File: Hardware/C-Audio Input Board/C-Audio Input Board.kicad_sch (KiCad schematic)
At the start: 5 parts

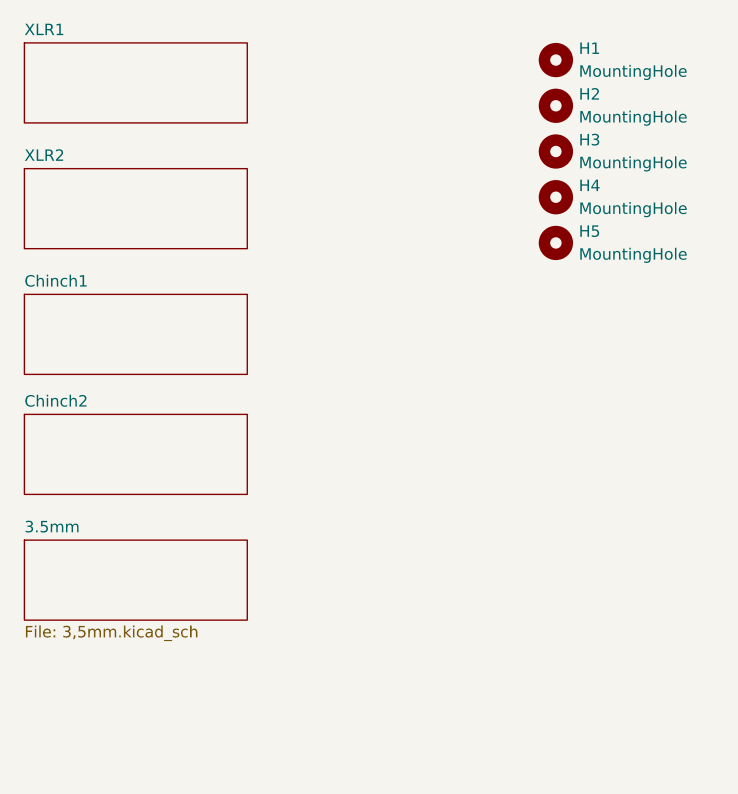
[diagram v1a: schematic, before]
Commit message: added pentaconn and silkscreen marking. Also added PCBWay logo for sponsorship
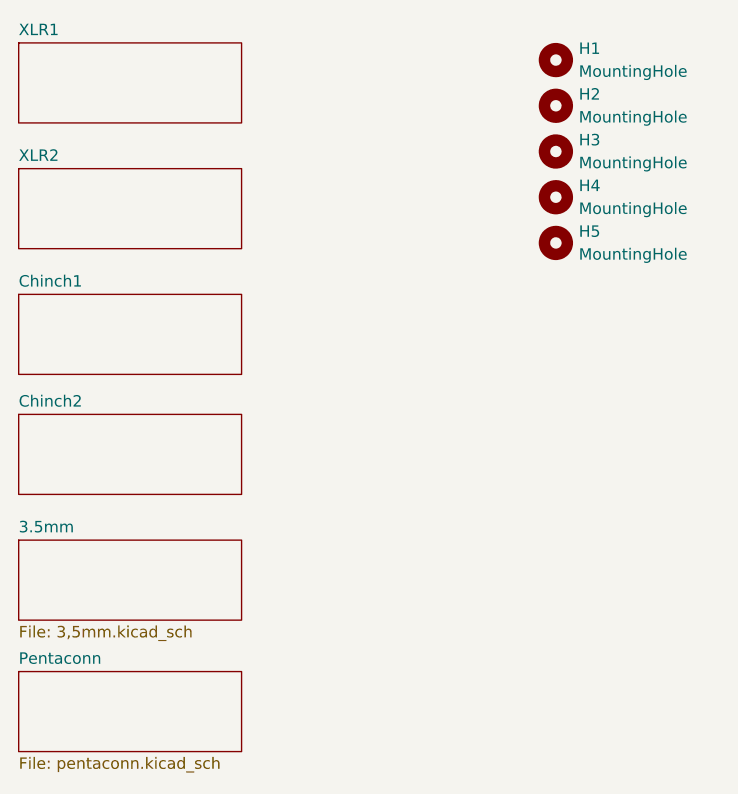
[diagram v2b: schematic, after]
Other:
- added sheet Pentaconn (pentaconn.kicad_sch)
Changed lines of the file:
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@@
 	)
 	(sheet
-		(at 41.275 76.835)
+		(at 40.64 76.835)
 		(size 24.765 8.89)
 		(exclude_from_sim no)
@@
 		)
 		(property "Sheetname" "Chinch2"
-			(at 41.275 76.1234 0)
+			(at 40.64 76.1234 0)
 			(effects
 				(font
@@
 		)
 		(property "Sheetfile" "chinch.kicad_sch"
-			(at 41.275 86.3096 0)
+			(at 40.64 86.3096 0)
 			(effects
 				(font
@@
 	)
 	(sheet
-		(at 41.275 90.805)
+		(at 40.64 90.805)
 		(size 24.765 8.89)
 		(exclude_from_sim no)
@@
 		)
 		(property "Sheetname" "3.5mm"
-			(at 41.275 90.0934 0)
+			(at 40.64 90.0934 0)
 			(effects
 				(font
@@
 		)
 		(property "Sheetfile" "3,5mm.kicad_sch"
-			(at 41.275 100.2796 0)
+			(at 40.64 100.2796 0)
 			(effects
 				(font
@@
 	)
 	(sheet
-		(at 41.275 35.56)
+		(at 40.64 35.56)
 		(size 24.765 8.89)
 		(exclude_from_sim no)
@@
 		)
 		(property "Sheetname" "XLR1"
-			(at 41.275 34.8484 0)
+			(at 40.64 34.8484 0)
 			(effects
 				(font
@@
 		)
 		(property "Sheetfile" "xlr.kicad_sch"
-			(at 41.275 45.0346 0)
+			(at 40.64 45.0346 0)
 			(effects
 				(font
@@
 	)
 	(sheet
-		(at 41.275 49.53)
+		(at 40.64 49.53)
 		(size 24.765 8.89)
 		(exclude_from_sim no)
@@
 		)
 		(property "Sheetname" "XLR2"
-			(at 41.275 48.8184 0)
+			(at 40.64 48.8184 0)
 			(effects
 				(font
@@
 		)
 		(property "Sheetfile" "xlr.kicad_sch"
-			(at 41.275 59.0046 0)
+			(at 40.64 59.0046 0)
 			(effects
 				(font
@@
 	)
 	(sheet
-		(at 41.275 63.5)
+		(at 40.64 105.41)
+		(size 24.765 8.89)
+		(exclude_from_sim no)
+		(in_bom yes)
+		(on_board yes)
+		(dnp no)
+		(fields_autoplaced yes)
+		(stroke
+			(width 0.1524)
+			(type solid)
+		)
+		(fill
+			(color 0 0 0 0.0000)
+		)
+		(property "Sheetname" "Pentaconn"
+			(at 40.64 104.6984 0)
+			(effects
+				(font
+					(size 1.27 1.27)
+				)
+				(justify left bottom)
+			)
+		)
+		(property "Sheetfile" "pentaconn.kicad_sch"
+			(at 40.64 114.8846 0)
+			(effects
+				(font
+					(size 1.27 1.27)
+				)
+				(justify left top)
+			)
+		)
+		(instances
+			(project "C-Audio Input Board"
+				(path "/b5cfd55f-d63e-4140-a74b-70044b12fe2d"
+					(page "7")
+				)
+			)
+		)
+	)
+	(sheet
+		(at 40.64 63.5)
 		(size 24.765 8.89)
 		(exclude_from_sim no)
@@
 		)
 		(property "Sheetname" "Chinch1"
-			(at 41.275 62.7884 0)
+			(at 40.64 62.7884 0)
 			(effects
 				(font
@@
 		)
 		(property "Sheetfile" "chinch.kicad_sch"
-			(at 41.275 72.9746 0)
-			(effects
-				(font
+			(at 40.64 72.9746 0)
+			(effects
+				(font
